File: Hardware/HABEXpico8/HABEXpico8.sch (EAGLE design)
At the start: 48 parts, among them Q1 2.5A/30V, SW1 SKQGADE010, SW2 SKQGADE010, U1 LTC3106, U2 EVA-8M, U3 STM32L011G4, U4 3.3V, Y1 ABS07-120-32.768KHZ-T

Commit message: Updated Power System, detailed GPS and MCU
Updated Power System, detailed GPS and MCU, removed backup files.
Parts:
- removed U$1: JTI_ANTENNA-1575AT43A40, habexpico8:JTI_ANTENNA-1575AT43A40
- added C16: 0.1uF, SparkFun-Capacitors:0.1UF-0603-25V-5%
- added C17, C18: 6pF, rcl:C-EUC0603
- added C19: 1.0uF, SparkFun-Capacitors:1.0UF-0603-16V-10%
- added C20: 10nF, SparkFun-Capacitors:10NF-0603-50V-10%
- added C21: 10uF, SparkFun-Capacitors:10UF-0603-6.3V-20%
- added C22: 10uF, SparkFun-Capacitors:10UF-0805-10V-10%
- added CR2: USBLC6-2SC6, habexpico8:USBLC6-2SC6
- added IC1: LT1763CS8-3.3, linear-technology:LT1763CS8-3.3
- added JP10, JP11, JP12, JP13, JP6, JP7, JP8, JP9: (no value), SparkFun-Retired:JUMPER-2PTH
- added JP14, JP15, JP4, JP5: JUMPER-SMT_2_NO_SILK, SparkFun-Jumpers:JUMPER-SMT_2_NO_SILK
- added L2: 33nH/±5%/500mA, SparkFun-Coils:INDUCTOR-0603-33NH
- added R11: 10, SparkFun-Resistors:10OHM-1206-1/4W-1%
- added R12: 10k, SparkFun-Resistors:10KOHM-0603-1/10W-1%
- added R13, R16: 27, SparkFun-Resistors:27OHM-0603-1/10W-1%
- added R14, R15: 5.1k 10%, SparkFun-Resistors:RESISTOR0603
- added U5: USB-C_R/A_HYBRID_RCPT, habexpico8:USB-C_R/A_HYBRID
- added U6: FT232RL, SparkFun-IC-Comms:FT232RLSSOP
- added X1, X2, X3, X4: BU-SMA-V, con-coax:BU-SMA-V
- added X5: JTI_ANTENNA-1575AT43A40, habexpico8:JTI_ANTENNA-1575AT43A40
- added X6: C-GRID-04-70553, con-molex:C-GRID-04-70553
- added X7: C-GRID-02-70553, con-molex:C-GRID-02-70553
- added Y2: ABS07-120-32.768KHZ-T, SparkFun-Clocks:CRYSTAL-32.768KHZSMD-3.2X1.5
- L1: value INDUCTOR-1210 -> 10uH
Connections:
- net +5V renamed USB_VBUS
- new net 5V: C19.1, IC1.!SHDN, IC1.IN, JP12.1, JP13.1
- new net N$12: C16.1, L2.1, R11.1
- new net N$13: C18.1, JP4.2, Y2.2
- new net N$14: L2.2, X2.1, X3.1
- new net N$15: CR2.I/O2, R13.1
- new net N$16: CR2.I/O1, R16.1
- new net N$19: C20.2, IC1.BYP
- new net REG_3.3V: C20.1, C21.1, IC1.OUT, IC1.SENSE, JP11.2
- new net RF_IN: U2.1_RF_IN, X1.1
- new net SER_DN: R13.2
- new net SER_DP: R16.2
- new net USBC_CC1: R14.2, U5.A5_CC1
- new net USBC_CC2: R15.2, U5.B5_CC2
- new net USBC_DN: CR2.I/O1_2, U5.A7_DN1, U5.B7_DN2
- new net USBC_DP: CR2.I/O2_2, U5.A6_DP1, U5.B6_DP2
- new net USBC_GND: JP14.1, U5.A12_GND, U5.A1_GND, U5.B12_GND, U5.B1_GND, U5.SHL
- new net USBC_VBUS: C22.1, CR2.VBUS, JP12.2, U5.A4_VBUS, U5.A9_VBUS, U5.B4_VBUS, U5.B9_VBUS
- new net USB_GND: J2.GND, J2.SHIELD, JP15.1
- new net VAUX_3.3V: JP10.2, X7-2.S
- new net VAUX_5V: JP13.2, X6-3.S, X6-4.S
- new net VSOLAR: C7.1, JP1.2, R1.2, SC1.VPOS, SC2.VPOS
- net 3.3V: now also J3.8, J4.8, JP10.1, JP11.1, R11.2, R12.2; no longer J3.6
- net GND: now also C16.2, C17.2, C18.2, C19.2, C21.2, C22.2, CR2.GND, IC1.GND@1, IC1.GND@2, IC1.GND@3, JP14.2, JP15.2, R14.1, R15.1, X1.2, X2.2, X3.2, X4.2, X6-1.S, X6-2.S, X7-1.S; no longer J2.GND, J2.SHIELD
- net GPS_EN: now also J4.5
- net GPS_RESET: now also J4.2, R12.1; no longer J4.4
- net GPS_RX: now also J4.3; no longer J4.2
- net GPS_TX: now also J4.4; no longer J4.3
- net MCU_OSC32_IN: now also JP5.1
- net MCU_OSC32_OUT: now also JP4.1
- net N$10: now also C17.1, JP5.2, Y2.1; no longer JP1.1, U1.VIN
- net N$4: now also X4.1, X5.FEED; no longer U$1.FEED, U2.1_RF_IN
- net VIN: now also JP1.1, U1.VIN; no longer C7.1, JP1.2, R1.2, SC1.VPOS, SC2.VPOS
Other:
- note added: "3. JP14 AND JP15 MUST BE JUMPERED FOR USB OPERATION 2. REFER TO MCU SUBSYSTEM (PAGE 4) FOR DATA SCHEMATIC 1. TO BE REPLACED WITH 6F SUPERCAP NOTES: THIS PAGE"
- note added: "3. RTC ENABLES POWER SAVE MODES 2. CRYSTAL 32.7680KHZ 6PF SMD, 3.20MM x 1.5MM 1. RESERVED NOTES: THIS PAGE"
- note added: "5"
- note added: "5. MOVE SMD ANT TO GPS MODULE FOR FLIGHT CONFIG 4. SHORT VDD_USB TO GND FOR FLIGHT CONFIG 3. RTC ENABLES POWER SAVE MODE, ALLOWS FOR GPS TRACKING USING ONLY SOLAR POWER 2. CRYSTAL 32.7680KHZ 6PF SMD, 3.20MM x 1.5MM 1. ENHANCEMENT-MODE P-CHANNEL MOSFET NOTES: THIS PAGE"
- note added: "5V REGULATOR"
- note added: "AUXILIARY +3.3V POWER"
- note added: "AUXILIARY +5V POWER"
- note added: "GPS ANTENNA ACTIVE/PASSIVE"
- note added: "GPS SUBSYSTEM"
- note added: "MCU SUBSYSTEM"
- note added: "POWER SOURCE JUMPERS"
- note added: "POWER SYSTEM"
- note added: "RADIO SUBSYSTEM"
- note added: "SINGLE POINT GROUND"
- note added: "TOP LEVEL DIAGRAM"
- note added: "UART GPS UART LOOPBACK/DEBUG CONSOLE SPI RADIO"
- note added: "USB-C CONNECTOR"
- note removed: "1. TO BE REPLACED WITH 6F SUPERCAP NOTES: THIS PAGE"
- note removed: "4. SHORT VDD_USB TO GND FOR FLIGHT 3. RTC ENABLES POWER SAVE MODE, ALLOWS FOR GPS TRACKING USING ONLY SOLAR POWER 2. CRYSTAL 32.7680KHZ 6PF SMD, 3.20MM x 1.5MM 1. ENHANCEMENT-MODE P-CHANNEL MOSFET NOTES: THIS PAGE"
- moved on the sheet: C1, C10, C13, C14, C15, C2, C3, C4, C5, C6, C7, C8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

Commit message: Added RF Front End w/ Simulation
Added RF Front End w/ Simulation
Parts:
- removed U$2: SI4464, habexpico8:SI4464
- added C0: 43pF, Nordic_nRF:CAPACITOR_0603_L
- added C23, C24, C27: 0.1uF, SparkFun-Capacitors:0.1UF-0603-25V-5%
- added C25: 10uF, SparkFun-Capacitors:10UF-0603-6.3V-20%
- added C26: 10nF, SparkFun-Capacitors:10NF-0603-50V-10%
- added C28, C29: 10pF, SparkFun-Capacitors:10PF-0603-50V-5%
- added C32: 15pF, Nordic_nRF:CAPACITOR_0603_L
- added C33, CM1: 8.2pF, Nordic_nRF:CAPACITOR_0603_L
- added D3: RED, SparkFun-LED:LED-RED0603
- added D4: GREEN, SparkFun-LED:LED-GREEN0603
- added JP16, JP17, JP18, JP19, JP20: JUMPER-3PTH, SparkFun-Retired:JUMPER-3PTH
- added L5, L6, LM1: 18nH, Nordic_nRF:INDUCTOR_0603_L
- added LC: 470nH, Nordic_nRF:INDUCTOR_0603_L
- added R17, R18: 300, SparkFun-Resistors:300OHM-0603-1/10W-1%
- added R19: 10k, SparkFun-Resistors:10KOHM-0603-1/10W-1%
- added R20, R21: 100k, SparkFun-Resistors:100KOHM-0603-1/10W-1%
- added SJ1, SJ2, SJ3, SJ4: SOLDERJUMPERNO, SparkFun-Retired:SOLDERJUMPERNO
- added TP1, TP2: TPPAD1-13, testpad:TPPAD1-13
- added U7: 3.3V, SparkFun-IC-Power:V_REG_AP2112K-3.3V
- added X8: 30MHZ 402F3001XIAR, IQD-Frequency-Products:CRYSTALS-GND-LID-IQXC-42
- added X9: BU-SMA-V, con-coax:BU-SMA-V
- JP14, JP15: value JUMPER-SMT_2_NO_SILK -> JUMPER-3PTH; device SparkFun-Jumpers:JUMPER-SMT_2_NO_SILK -> SparkFun-Retired:JUMPER-3PTH
- JP6, JP7, JP8, JP9: value (none) -> JUMPER-3PTH; device SparkFun-Retired:JUMPER-2PTH -> SparkFun-Retired:JUMPER-3PTH
- U4: value 3.3V -> SI4464; device SparkFun-IC-Power:V_REG_AP2112K-3.3V -> habexpico8:SI4464
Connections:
- removed net USBC_GND: JP14.1, U5.A12_GND, U5.A1_GND, U5.B12_GND, U5.B1_GND, U5.SHL
- removed net USB_GND: J2.GND, J2.SHIELD, JP15.1
- new net FTDI_SER_RXD: JP9.1, U6.RXD
- new net FTDI_SER_TXD: JP8.1, U6.TXD
- new net LPUART1_RX: JP6.2, JP6.3, U3.PA3
- new net LPUART1_TX: JP7.2, JP7.3, U3.PA2
- new net MCU_RADIO_EN: JP20.2, JP20.3, U3.PA8
- new net MCU_RADIO_GPIO1: JP19.2, JP19.3, U3.PB1
- new net MCU_RADIO_NIRQ: JP18.2, JP18.3, U3.PB0
- new net N$17: D3.C, U6.TXLED
- new net N$18: D4.C, U6.RXLED
- new net N$20: D3.A, R17.1
- new net N$21: D4.A, R18.1
- new net N$22: SJ1.2, U6.VCCIO
- new net N$23: R17.2, SJ2.1
- new net N$24: R18.2, SJ3.1
- new net N$25: R11.2, SJ4.1
- new net N$26: C28.1, TP1.TP, U4.XIN, X8.3
- new net N$27: C29.1, TP2.TP, U4.XOUT, X8.1
- new net N$28: C0.1, LC.2, U4.TX
- new net N$29: CM1.1, L5.2, LM1.1
- new net N$30: C0.2, LM1.2
- new net N$31: C32.1, L5.1, L6.2
- new net RADIO_EN: JP20.1, R21.1, U4.SDN
- new net RADIO_GPIO1: JP19.1, R20.1, U4.GPIO1
- new net RADIO_MISO: JP16.1, U4.SDO
- new net RADIO_MOSI: JP17.1, U4.SDI
- new net RADIO_NIRQ: JP18.1, U4.NIRQ
- new net RADIO_NSS: JP14.1, U4.NSEL
- new net RADIO_SCLK: JP15.1, U4.SCLK
- new net RF_OUT: C33.1, L6.1, X9.1
- new net SPI1_MISO: JP16.2, JP16.3, U3.PA6
- new net SPI1_MOSI: JP17.2, JP17.3, U3.PA7
- new net SPI1_NSS: JP14.2, JP14.3, U3.PA4
- new net SPI1_SCK: JP15.2, JP15.3, U3.PA5
- new net USART2_RX: JP8.2, JP8.3, U3.PA10
- new net USART2_TX: JP9.2, JP9.3, U3.PA9
- net 3.3V: now also C23.1, C25.1, C26.1, C27.1, LC.1, R20.2, R21.2, SJ1.1, SJ2.2, SJ3.2, SJ4.2, SW1.A1, U4.VDD, U4.VDD2; no longer R11.2
- net GND: now also C23.2, C24.2, C25.2, C26.2, C27.2, C28.2, C29.2, C32.2, C33.2, CM1.2, J2.GND, J2.SHIELD, R14.2, R15.2, R19.1, U4.GND2, U5.A12_GND, U5.A1_GND, U5.B12_GND, U5.B1_GND, U5.SHL, U6.AGND, U6.GND18, U6.GND21, U6.GND7, U6.TEST, U7.GND, X9.2; no longer JP14.2, JP15.2, R14.1, R15.1, SW1.B1
- net GPS_EN: now also U3.PA1
- net GPS_RX: now also JP7.1
- net GPS_TX: now also JP6.1
- net GPS_USB_VDD: now also U7.OUT; no longer U4.OUT
- net MCU_RESET: now also R19.2, SW1.B1; no longer SW1.A1
- net SER_DN: now also U6.USBDM
- net SER_DP: now also U6.USBDP
- net USBC_CC1: now also R14.1; no longer R14.2
- net USBC_CC2: now also R15.1; no longer R15.2
- net USBC_VBUS: now also C24.1, U6.VCC
- net USB_VBUS: now also U7.EN, U7.IN; no longer U4.EN, U4.IN
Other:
- note added: "2. SEE MCU SUBSYSTEM (PAGE 4) FOR SERIAL INTERFACE 1. TO BE REPLACED WITH 6F SUPERCAP NOTES: THIS PAGE"
- note added: "3. REFERENCE DOCUMENT "AN627: SI4460/61/67 LOW-POWER PA MATCHING" FOR COMPONENT VALUES TABLE 14. FOR MATCH NETWORK COMPONENT VALUES APPROXIMATIONS, SEE SIMULATION "RF_FRONT_END" FOR EXACT SECTION 3.1.1.1 FOR LCHOKE 2. 50 OHM LOAD 1. CRYSTAL 30.000MHZ 10PF SMD, 2.00MM x 1.6MM, LOAD CAP OPTIONAL NOTES: THIS PAGE"
- note added: "5. JUMP SJ1, SJ2, AND SJ3 FOR SERIAL OPERATION 4. SEE POWER SYSTEM (PAGE 2) FOR USB-C CONNECTOR 3. RTC ENABLES POWER SAVE MODES 2. CRYSTAL 32.7680KHZ 6PF SMD, 3.20MM x 1.5MM 1. RESERVED NOTES: THIS PAGE"
- note added: "6"
- note added: "6. JUMP SJ4 FOR ACTIVE ANTENNA 5. MOVE SMD ANT TO GPS MODULE FOR FLIGHT CONFIG 4. SHORT VDD_USB TO GND FOR FLIGHT CONFIG 3. RTC ENABLES POWER SAVE MODE, ALLOWS FOR GPS TRACKING USING ONLY SOLAR POWER 2. CRYSTAL 32.7680KHZ 6PF SMD, 3.20MM x 1.5MM 1. ENHANCEMENT-MODE P-CHANNEL MOSFET NOTES: THIS PAGE"
- note added: "MCU EXTERNAL OSCILLATOR"
- note added: "MCU JUMPERS & TEST POINTS"
- note added: "MCU SERIAL INTERFACE"
- note added: "UART1: GPS UART2: SERIAL/DEBUG CONSOLE SPI1: RADIO"
- note added: "USB-C CONNECTOR - SERIAL DEBUG"
- note removed: "3. JP14 AND JP15 MUST BE JUMPERED FOR USB OPERATION 2. REFER TO MCU SUBSYSTEM (PAGE 4) FOR DATA SCHEMATIC 1. TO BE REPLACED WITH 6F SUPERCAP NOTES: THIS PAGE"
- note removed: "3. RTC ENABLES POWER SAVE MODES 2. CRYSTAL 32.7680KHZ 6PF SMD, 3.20MM x 1.5MM 1. RESERVED NOTES: THIS PAGE"
- note removed: "5. MOVE SMD ANT TO GPS MODULE FOR FLIGHT CONFIG 4. SHORT VDD_USB TO GND FOR FLIGHT CONFIG 3. RTC ENABLES POWER SAVE MODE, ALLOWS FOR GPS TRACKING USING ONLY SOLAR POWER 2. CRYSTAL 32.7680KHZ 6PF SMD, 3.20MM x 1.5MM 1. ENHANCEMENT-MODE P-CHANNEL MOSFET NOTES: THIS PAGE"
- note removed: "SINGLE POINT GROUND"
- note removed: "UART GPS UART LOOPBACK/DEBUG CONSOLE SPI RADIO"
- note removed: "USB-C CONNECTOR"

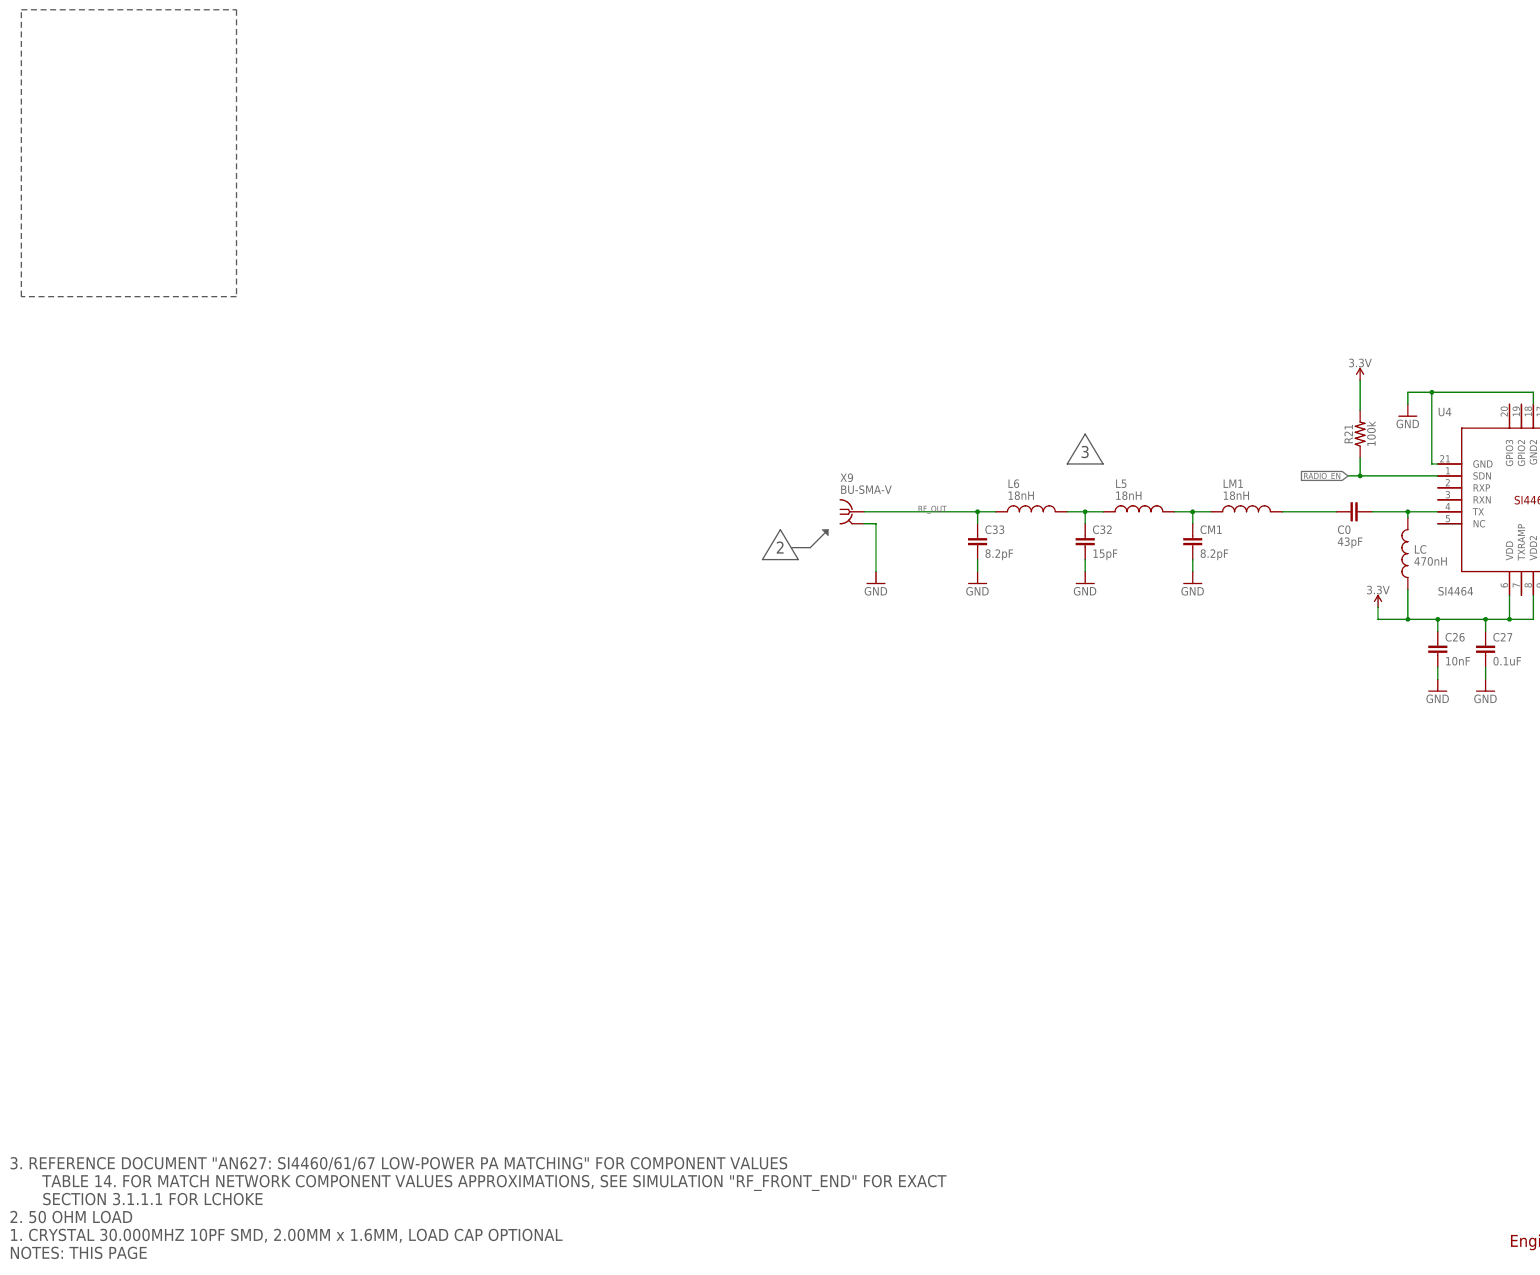
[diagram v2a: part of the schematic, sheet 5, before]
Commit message: Finished schematic and simulations
Finished schematic and simulations. Expecting to make small tweaks in
future revisions.
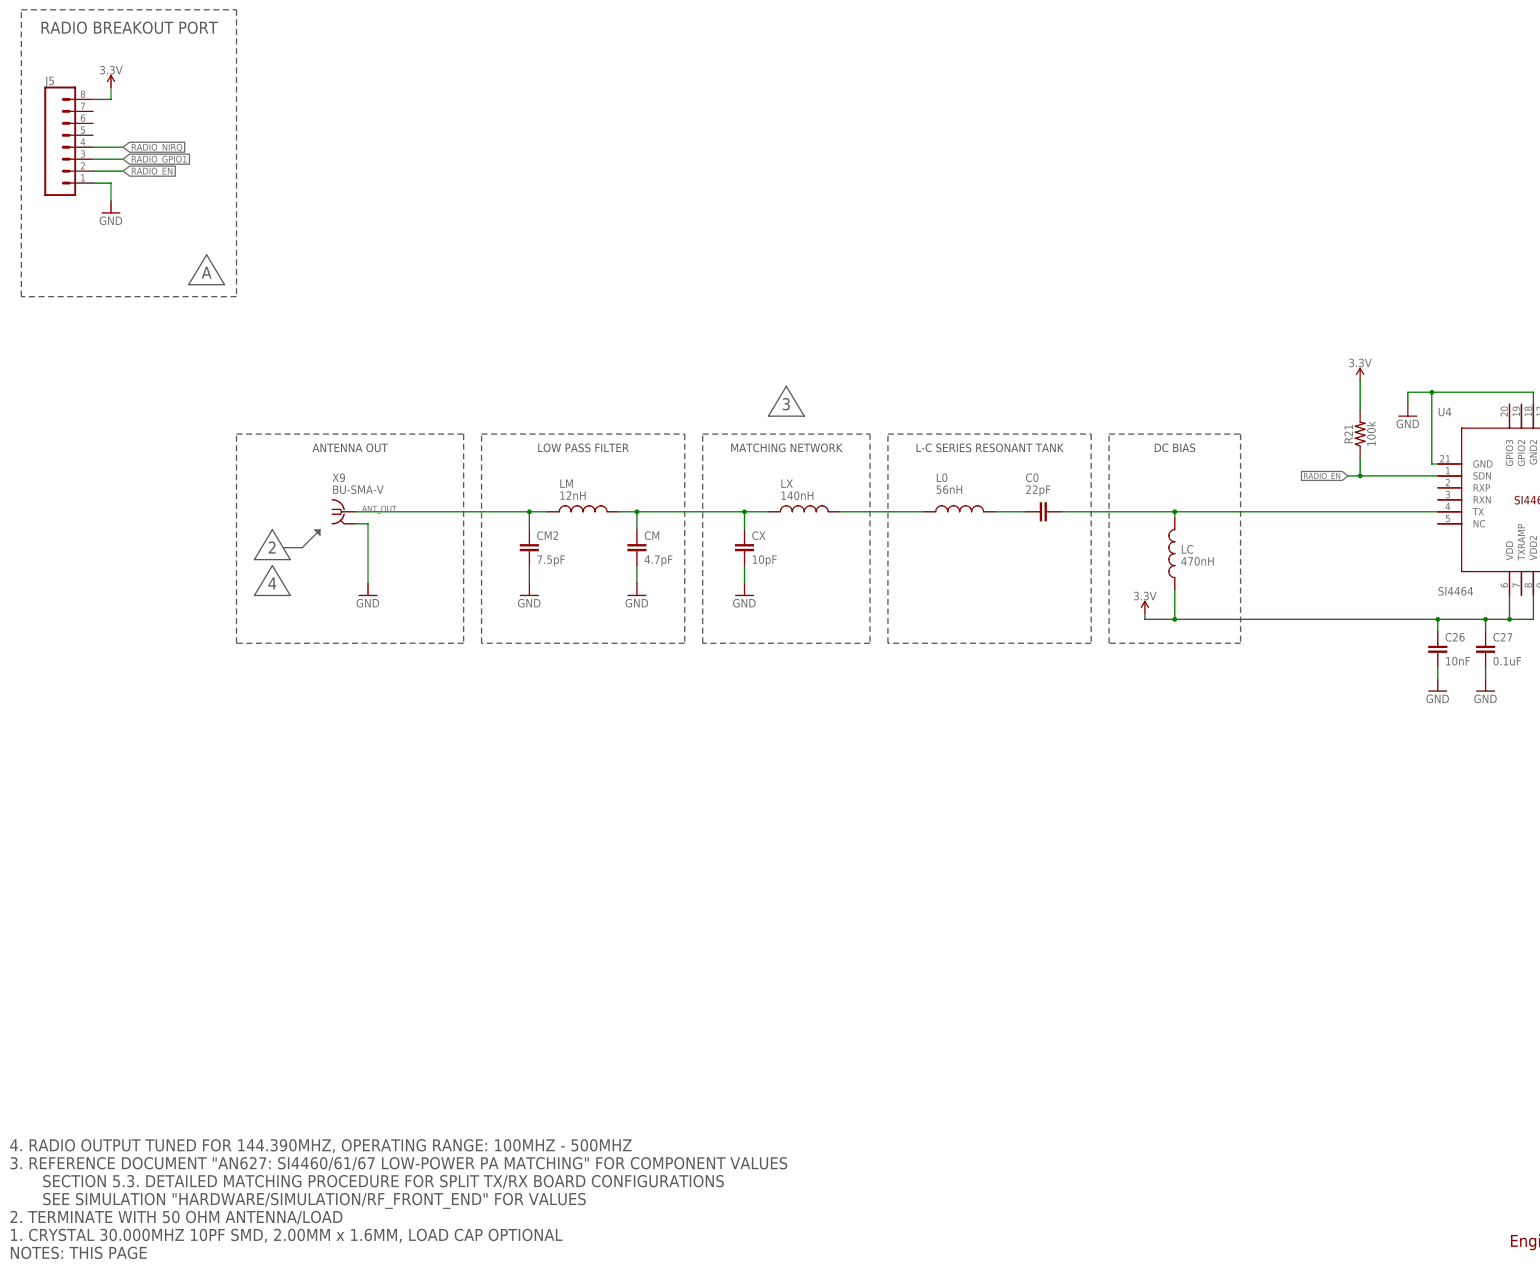
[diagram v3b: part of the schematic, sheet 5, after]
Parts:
- removed C32: 15pF, Nordic_nRF:CAPACITOR_0603_L
- removed C33, CM1: 8.2pF, Nordic_nRF:CAPACITOR_0603_L
- removed L5, L6, LM1: 18nH, Nordic_nRF:INDUCTOR_0603_L
- added CM: 4.7pF, Nordic_nRF:CAPACITOR_0603_L
- added CM2: 7.5pF, Nordic_nRF:CAPACITOR_0603_L
- added CX: 10pF, Nordic_nRF:CAPACITOR_0603_L
- added J5: (no value), SparkFun-Connectors:CONN_08"
- added L0: 56nH, Nordic_nRF:INDUCTOR_0603_L
- added LM: 12nH, Nordic_nRF:INDUCTOR_0603_L
- added LX: 140nH, Nordic_nRF:INDUCTOR_0603_L
- C0: value 43pF -> 22pF
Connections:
- removed net RF_OUT: C33.1, L6.1, X9.1
- new net ANT_OUT: CM2.1, LM.1, X9.1
- net 3.3V: now also J5.8
- net GND: now also CM.2, CM2.2, CX.2, J5.1; no longer C32.2, C33.2, CM1.2
- net N$29: now also L0.1, LX.2; no longer CM1.1, L5.2, LM1.1
- net N$30: now also L0.2; no longer LM1.2
- net N$31: now also CM.1, CX.1, LM.2, LX.1; no longer C32.1, L5.1, L6.2
- net RADIO_EN: now also J5.2
- net RADIO_GPIO1: now also J5.3
- net RADIO_NIRQ: now also J5.4
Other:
- note added: "+3.3V"
- note added: "4. RADIO OUTPUT TUNED FOR 144.390MHZ, OPERATING RANGE: 100MHZ - 500MHZ 3. REFERENCE DOCUMENT "AN627: SI4460/61/67 LOW-POWER PA MATCHING" FOR COMPONENT VALUES SECTION 5.3. DETAILED MATCHING PROCEDURE FOR SPLIT TX/RX BOARD CONFIGURATIONS SEE SIMULATION "HARDWARE/SIMULATION/RF_FRONT_END" FOR VALUES 2. TERMINATE WITH 50 OHM ANTENNA/LOAD 1. CRYSTAL 30.000MHZ 10PF SMD, 2.00MM x 1.6MM, LOAD CAP OPTIONAL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"
- note added: "6. DEVICE INTERFACES UART1: GPS UART2: SERIAL DEBUG CONSOLE SPI1: RADIO 5. JUMP SJ1, SJ2, AND SJ3 FOR SERIAL OPERATION 4. SEE POWER SYSTEM (PAGE 2) FOR USB-C CONNECTOR 3. RTC ENABLES POWER SAVE MODES 2. CRYSTAL 32.7680KHZ 6PF SMD, 3.20MM x 1.5MM 1. RESERVED NOTES: THIS PAGE"
- note added: "ANTENNA OUT"
- note added: "COMPUTE ELEMENT"
- note added: "DC BIAS"
- note added: "DEBUGGER"
- note added: "GSE"
- note added: "L-C SERIES RESONANT TANK"
- note added: "LOW PASS FILTER"
- note added: "MATCHING NETWORK"
- note added: "PAYLOAD"
- note added: "RADIO BREAKOUT PORT"
- note added: "SERIAL TERMINAL"
- note added: "SOLAR"
- note added: "SPI1"
- note added: "STORAGE"
- note added: "SW-DP"
- note added: "UART1"
- note added: "UART2"
- note removed: "3. REFERENCE DOCUMENT "AN627: SI4460/61/67 LOW-POWER PA MATCHING" FOR COMPONENT VALUES TABLE 14. FOR MATCH NETWORK COMPONENT VALUES APPROXIMATIONS, SEE SIMULATION "RF_FRONT_END" FOR EXACT SECTION 3.1.1.1 FOR LCHOKE 2. 50 OHM LOAD 1. CRYSTAL 30.000MHZ 10PF SMD, 2.00MM x 1.6MM, LOAD CAP OPTIONAL NOTES: THIS PAGE"
- note removed: "5. JUMP SJ1, SJ2, AND SJ3 FOR SERIAL OPERATION 4. SEE POWER SYSTEM (PAGE 2) FOR USB-C CONNECTOR 3. RTC ENABLES POWER SAVE MODES 2. CRYSTAL 32.7680KHZ 6PF SMD, 3.20MM x 1.5MM 1. RESERVED NOTES: THIS PAGE"
- note removed: "UART1: GPS UART2: SERIAL/DEBUG CONSOLE SPI1: RADIO"
- moved on the sheet: C0, LC, X9
